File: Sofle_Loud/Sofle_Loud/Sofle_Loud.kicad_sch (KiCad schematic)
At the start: 76 parts, among them J1 Pimaroni Trackball, J2 4PIN, J3 OLED, Q2 TIP120, SW1 SW_PUSH_LED, SW10 SW_PUSH_LED, SW11 SW_PUSH_LED, SW12 SW_PUSH_LED, SW13 SW_PUSH_LED, SW14 SW_PUSH_LED, SW15 SW_PUSH_LED, SW16 SW_PUSH_LED, SW17 SW_PUSH_LED, SW18 SW_PUSH_LED, SW19 SW_PUSH_LED, SW2 SW_PUSH_LED, SW20 SW_PUSH_LED, SW21 SW_PUSH_LED, SW22 SW_PUSH_LED, SW23 SW_PUSH_LED, SW24 SW_PUSH_LED, SW25 Rotary_Encoder_Switch, SW26 SW_PUSH_LED, SW27 SW_PUSH_LED, SW28 SW_PUSH_LED, SW29 SW_PUSH_LED, SW3 SW_PUSH_LED, SW30 SW_PUSH_LED, SW4 SW_PUSH_LED, SW5 SW_PUSH_LED, SW6 SW_PUSH_LED, SW7 SW_PUSH_LED, SW8 SW_PUSH_LED, SW9 SW_PUSH_LED, U1 ProMicro_Choc_MX

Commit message: Updated transistor footprint Added extra room for heatsink Rebuilt outline Wired solenoid and piezzo
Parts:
- Q2: footprint Package_TO_SOT_THT:TO-220-3_Horizontal_TabUp -> SofleChocLoud:TO-220-3_Horizontal_TabUp
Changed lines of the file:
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@@
       (effects (font (size 1.27 1.27)) (justify left))
     )
-    (property "Footprint" "Package_TO_SOT_THT:TO-220-3_Horizontal_TabUp" (at 46.99 135.255 0)
+    (property "Footprint" "SofleChocLoud:TO-220-3_Horizontal_TabUp" (at 46.99 135.255 0)
       (effects (font (size 1.27 1.27) italic) (justify left) hide)
     )

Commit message: Footprint cleanup for plates Added markings to OLEDs indicating screen start/end offset oleds 3mm from edge of board rotated transistor for more slop on heatsinks Created Double sided TRRS footprint Moved Pimaroni closer to OLED footprint diode routing cleanup
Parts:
- J2: footprint SofleChocLoud:MJ-4PP-9_Choc_MX -> SofleChocLoud:TRRS_or_TRS_Sofle_Click
- J_SOL_1: footprint Connector_PinHeader_2.54mm:PinHeader_1x02_P2.54mm_Vertical -> SofleChocLoud:PinHeader_1x02_P2.54mm_L-Shaped
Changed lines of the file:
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@@
       (effects (font (size 1.524 1.524)))
     )
-    (property "Footprint" "SofleChocLoud:MJ-4PP-9_Choc_MX" (at 82.55 78.74 0)
+    (property "Footprint" "SofleChocLoud:TRRS_or_TRS_Sofle_Click" (at 82.55 78.74 0)
       (effects (font (size 1.524 1.524)) hide)
     )
@@
       (effects (font (size 1.27 1.27)))
     )
-    (property "Footprint" "Connector_PinHeader_2.54mm:PinHeader_1x02_P2.54mm_Vertical" (at 30.48 123.19 0)
-      (effects (font (size 1.27 1.27)) hide)
-    )
+    (property "Footprint" "SofleChocLoud:PinHeader_1x02_P2.54mm_L-Shaped" (at 30.48 123.19 0)
+      (effects (font (size 1.27 1.27)) hide)
+    )

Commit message: Adding 2nd tier keyplate
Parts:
- TH1, TH2, TH3, TH4, TH5, TH6, TH7: footprint SofleChocLoud:M2_HOLE_PCB -> SofleChocLoud:M2_HOLE_PCB_through_hole
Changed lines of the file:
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@@
       (effects (font (size 1.524 1.524)))
     )
-    (property "Footprint" "SofleChocLoud:M2_HOLE_PCB" (at 19.05 190.5 0)
+    (property "Footprint" "SofleChocLoud:M2_HOLE_PCB_through_hole" (at 19.05 190.5 0)
       (effects (font (size 1.524 1.524)) hide)
     )
@@
       (effects (font (size 1.524 1.524)))
     )
-    (property "Footprint" "SofleChocLoud:M2_HOLE_PCB" (at 27.94 190.5 0)
+    (property "Footprint" "SofleChocLoud:M2_HOLE_PCB_through_hole" (at 27.94 190.5 0)
       (effects (font (size 1.524 1.524)) hide)
     )
@@
       (effects (font (size 1.524 1.524)))
     )
-    (property "Footprint" "SofleChocLoud:M2_HOLE_PCB" (at 53.34 190.5 0)
+    (property "Footprint" "SofleChocLoud:M2_HOLE_PCB_through_hole" (at 53.34 190.5 0)
       (effects (font (size 1.524 1.524)) hide)
     )
@@
       (effects (font (size 1.524 1.524)))
     )
-    (property "Footprint" "SofleChocLoud:M2_HOLE_PCB" (at 62.23 190.5 0)
+    (property "Footprint" "SofleChocLoud:M2_HOLE_PCB_through_hole" (at 62.23 190.5 0)
       (effects (font (size 1.524 1.524)) hide)
     )
@@
       (effects (font (size 1.524 1.524)))
     )
-    (property "Footprint" "SofleChocLoud:M2_HOLE_PCB" (at 71.12 190.5 0)
+    (property "Footprint" "SofleChocLoud:M2_HOLE_PCB_through_hole" (at 71.12 190.5 0)
       (effects (font (size 1.524 1.524)) hide)
     )
@@
       (effects (font (size 1.524 1.524)))
     )
-    (property "Footprint" "SofleChocLoud:M2_HOLE_PCB" (at 80.01 190.5 0)
+    (property "Footprint" "SofleChocLoud:M2_HOLE_PCB_through_hole" (at 80.01 190.5 0)
       (effects (font (size 1.524 1.524)) hide)
     )
@@
       (effects (font (size 1.524 1.524)))
     )
-    (property "Footprint" "SofleChocLoud:M2_HOLE_PCB" (at 44.45 190.5 0)
+    (property "Footprint" "SofleChocLoud:M2_HOLE_PCB_through_hole" (at 44.45 190.5 0)
       (effects (font (size 1.524 1.524)) hide)
     )

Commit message: Updated pimoroni markings Added 3d models to components
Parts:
- D1, D10, D11, D12, D13, D14, D15, D16, D17, D18, D19, D2, D20, D21, D22, D23, D24, D25, D26, D27, D28, D29, D3, D30, D4, D5, D6, D7, D8, D9: footprint SofleChocLoud:D_SOD-123_DO-35_Hybrid_DoubleSided -> SofleChocLoud:D_SOD-123_DO-35_Hybrid_DoubleSided_V2
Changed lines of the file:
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@@
       (effects (font (size 1.27 1.27)) (justify right))
     )
-    (property "Footprint" "SofleChocLoud:D_SOD-123_DO-35_Hybrid_DoubleSided" (at 175.26 91.44 0)
+    (property "Footprint" "SofleChocLoud:D_SOD-123_DO-35_Hybrid_DoubleSided_V2" (at 175.26 91.44 0)
       (effects (font (size 1.27 1.27)) hide)
     )
@@
       (effects (font (size 1.27 1.27)) (justify right))
     )
-    (property "Footprint" "SofleChocLoud:D_SOD-123_DO-35_Hybrid_DoubleSided" (at 195.58 91.44 0)
+    (property "Footprint" "SofleChocLoud:D_SOD-123_DO-35_Hybrid_DoubleSided_V2" (at 195.58 91.44 0)
       (effects (font (size 1.27 1.27)) hide)
     )
@@
       (effects (font (size 1.27 1.27)) (justify right))
     )
-    (property "Footprint" "SofleChocLoud:D_SOD-123_DO-35_Hybrid_DoubleSided" (at 215.9 91.44 0)
+    (property "Footprint" "SofleChocLoud:D_SOD-123_DO-35_Hybrid_DoubleSided_V2" (at 215.9 91.44 0)
       (effects (font (size 1.27 1.27)) hide)
     )
@@
       (effects (font (size 1.27 1.27)) (justify right))
     )
-    (property "Footprint" "SofleChocLoud:D_SOD-123_DO-35_Hybrid_DoubleSided" (at 236.22 91.44 0)
+    (property "Footprint" "SofleChocLoud:D_SOD-123_DO-35_Hybrid_DoubleSided_V2" (at 236.22 91.44 0)
       (effects (font (size 1.27 1.27)) hide)
     )
@@
       (effects (font (size 1.27 1.27)) (justify right))
     )
-    (property "Footprint" "SofleChocLoud:D_SOD-123_DO-35_Hybrid_DoubleSided" (at 256.54 91.44 0)
+    (property "Footprint" "SofleChocLoud:D_SOD-123_DO-35_Hybrid_DoubleSided_V2" (at 256.54 91.44 0)
       (effects (font (size 1.27 1.27)) hide)
     )
@@
       (effects (font (size 1.27 1.27)) (justify right))
     )
-    (property "Footprint" "SofleChocLoud:D_SOD-123_DO-35_Hybrid_DoubleSided" (at 276.86 91.44 0)
+    (property "Footprint" "SofleChocLoud:D_SOD-123_DO-35_Hybrid_DoubleSided_V2" (at 276.86 91.44 0)
       (effects (font (size 1.27 1.27)) hide)
     )
@@
       (effects (font (size 1.27 1.27)) (justify right))
     )
-    (property "Footprint" "SofleChocLoud:D_SOD-123_DO-35_Hybrid_DoubleSided" (at 175.26 107.95 0)
+    (property "Footprint" "SofleChocLoud:D_SOD-123_DO-35_Hybrid_DoubleSided_V2" (at 175.26 107.95 0)
       (effects (font (size 1.27 1.27)) hide)
     )
@@
       (effects (font (size 1.27 1.27)) (justify right))
     )
-    (property "Footprint" "SofleChocLoud:D_SOD-123_DO-35_Hybrid_DoubleSided" (at 195.58 107.95 0)
+    (property "Footprint" "SofleChocLoud:D_SOD-123_DO-35_Hybrid_DoubleSided_V2" (at 195.58 107.95 0)
       (effects (font (size 1.27 1.27)) hide)
     )
@@
       (effects (font (size 1.27 1.27)) (justify right))
     )
-    (property "Footprint" "SofleChocLoud:D_SOD-123_DO-35_Hybrid_DoubleSided" (at 215.9 107.95 0)
+    (property "Footprint" "SofleChocLoud:D_SOD-123_DO-35_Hybrid_DoubleSided_V2" (at 215.9 107.95 0)
       (effects (font (size 1.27 1.27)) hide)
     )
@@
       (effects (font (size 1.27 1.27)) (justify right))
     )
-    (property "Footprint" "SofleChocLoud:D_SOD-123_DO-35_Hybrid_DoubleSided" (at 236.22 107.95 0)
+    (property "Footprint" "SofleChocLoud:D_SOD-123_DO-35_Hybrid_DoubleSided_V2" (at 236.22 107.95 0)
       (effects (font (size 1.27 1.27)) hide)
     )
@@
       (effects (font (size 1.27 1.27)) (justify right))
     )
-    (property "Footprint" "SofleChocLoud:D_SOD-123_DO-35_Hybrid_DoubleSided" (at 256.54 107.95 0)
+    (property "Footprint" "SofleChocLoud:D_SOD-123_DO-35_Hybrid_DoubleSided_V2" (at 256.54 107.95 0)
       (effects (font (size 1.27 1.27)) hide)
     )
@@
       (effects (font (size 1.27 1.27)) (justify right))
     )
-    (property "Footprint" "SofleChocLoud:D_SOD-123_DO-35_Hybrid_DoubleSided" (at 276.86 107.95 0)
+    (property "Footprint" "SofleChocLoud:D_SOD-123_DO-35_Hybrid_DoubleSided_V2" (at 276.86 107.95 0)
       (effects (font (size 1.27 1.27)) hide)
     )
@@
       (effects (font (size 1.27 1.27)) (justify right))
     )
-    (property "Footprint" "SofleChocLoud:D_SOD-123_DO-35_Hybrid_DoubleSided" (at 175.26 124.46 0)
+    (property "Footprint" "SofleChocLoud:D_SOD-123_DO-35_Hybrid_DoubleSided_V2" (at 175.26 124.46 0)
       (effects (font (size 1.27 1.27)) hide)
     )
@@
       (effects (font (size 1.27 1.27)) (justify right))
     )
-    (property "Footprint" "SofleChocLoud:D_SOD-123_DO-35_Hybrid_DoubleSided" (at 195.58 124.46 0)
+    (property "Footprint" "SofleChocLoud:D_SOD-123_DO-35_Hybrid_DoubleSided_V2" (at 195.58 124.46 0)
       (effects (font (size 1.27 1.27)) hide)
     )
@@
       (effects (font (size 1.27 1.27)) (justify right))
     )
-    (property "Footprint" "SofleChocLoud:D_SOD-123_DO-35_Hybrid_DoubleSided" (at 215.9 124.46 0)
+    (property "Footprint" "SofleChocLoud:D_SOD-123_DO-35_Hybrid_DoubleSided_V2" (at 215.9 124.46 0)
       (effects (font (size 1.27 1.27)) hide)
     )
@@
       (effects (font (size 1.27 1.27)) (justify right))
     )
-    (property "Footprint" "SofleChocLoud:D_SOD-123_DO-35_Hybrid_DoubleSided" (at 236.22 124.46 0)
+    (property "Footprint" "SofleChocLoud:D_SOD-123_DO-35_Hybrid_DoubleSided_V2" (at 236.22 124.46 0)
       (effects (font (size 1.27 1.27)) hide)
     )
@@
       (effects (font (size 1.27 1.27)) (justify right))
     )
-    (property "Footprint" "SofleChocLoud:D_SOD-123_DO-35_Hybrid_DoubleSided" (at 256.54 124.46 0)
+    (property "Footprint" "SofleChocLoud:D_SOD-123_DO-35_Hybrid_DoubleSided_V2" (at 256.54 124.46 0)
       (effects (font (size 1.27 1.27)) hide)
     )
@@
       (effects (font (size 1.27 1.27)) (justify right))
     )
-    (property "Footprint" "SofleChocLoud:D_SOD-123_DO-35_Hybrid_DoubleSided" (at 276.86 124.46 0)
+    (property "Footprint" "SofleChocLoud:D_SOD-123_DO-35_Hybrid_DoubleSided_V2" (at 276.86 124.46 0)
       (effects (font (size 1.27 1.27)) hide)
     )
@@
       (effects (font (size 1.27 1.27)) (justify right))
     )
-    (property "Footprint" "SofleChocLoud:D_SOD-123_DO-35_Hybrid_DoubleSided" (at 175.26 140.97 0)
+    (property "Footprint" "SofleChocLoud:D_SOD-123_DO-35_Hybrid_DoubleSided_V2" (at 175.26 140.97 0)
       (effects (font (size 1.27 1.27)) hide)
     )
@@
       (effects (font (size 1.27 1.27)) (justify right))
     )
-    (property "Footprint" "SofleChocLoud:D_SOD-123_DO-35_Hybrid_DoubleSided" (at 195.58 140.97 0)
+    (property "Footprint" "SofleChocLoud:D_SOD-123_DO-35_Hybrid_DoubleSided_V2" (at 195.58 140.97 0)
       (effects (font (size 1.27 1.27)) hide)
     )
@@
       (effects (font (size 1.27 1.27)) (justify right))
     )
-    (property "Footprint" "SofleChocLoud:D_SOD-123_DO-35_Hybrid_DoubleSided" (at 215.9 140.97 0)
+    (property "Footprint" "SofleChocLoud:D_SOD-123_DO-35_Hybrid_DoubleSided_V2" (at 215.9 140.97 0)
       (effects (font (size 1.27 1.27)) hide)
     )
@@
       (effects (font (size 1.27 1.27)) (justify right))
     )
-    (property "Footprint" "SofleChocLoud:D_SOD-123_DO-35_Hybrid_DoubleSided" (at 236.22 140.97 0)
+    (property "Footprint" "SofleChocLoud:D_SOD-123_DO-35_Hybrid_DoubleSided_V2" (at 236.22 140.97 0)
       (effects (font (size 1.27 1.27)) hide)
     )
@@
       (effects (font (size 1.27 1.27)) (justify right))
     )
-    (property "Footprint" "SofleChocLoud:D_SOD-123_DO-35_Hybrid_DoubleSided" (at 256.54 140.97 0)
+    (property "Footprint" "SofleChocLoud:D_SOD-123_DO-35_Hybrid_DoubleSided_V2" (at 256.54 140.97 0)
       (effects (font (size 1.27 1.27)) hide)
     )
@@
       (effects (font (size 1.27 1.27)) (justify right))
     )
-    (property "Footprint" "SofleChocLoud:D_SOD-123_DO-35_Hybrid_DoubleSided" (at 276.86 140.97 0)
+    (property "Footprint" "SofleChocLoud:D_SOD-123_DO-35_Hybrid_DoubleSided_V2" (at 276.86 140.97 0)
       (effects (font (size 1.27 1.27)) hide)
     )
@@
       (effects (font (size 1.27 1.27)) (justify right))
     )
-    (property "Footprint" "SofleChocLoud:D_SOD-123_DO-35_Hybrid_DoubleSided" (at 175.26 157.48 0)
+    (property "Footprint" "SofleChocLoud:D_SOD-123_DO-35_Hybrid_DoubleSided_V2" (at 175.26 157.48 0)
       (effects (font (size 1.27 1.27)) hide)
     )
@@
       (effects (font (size 1.27 1.27)) (justify right))
     )
-    (property "Footprint" "SofleChocLoud:D_SOD-123_DO-35_Hybrid_DoubleSided" (at 195.58 157.48 0)
+    (property "Footprint" "SofleChocLoud:D_SOD-123_DO-35_Hybrid_DoubleSided_V2" (at 195.58 157.48 0)
       (effects (font (size 1.27 1.27)) hide)
     )
@@
       (effects (font (size 1.27 1.27)) (justify right))
     )
-    (property "Footprint" "SofleChocLoud:D_SOD-123_DO-35_Hybrid_DoubleSided" (at 215.9 157.48 0)
+    (property "Footprint" "SofleChocLoud:D_SOD-123_DO-35_Hybrid_DoubleSided_V2" (at 215.9 157.48 0)
       (effects (font (size 1.27 1.27)) hide)
     )
@@
       (effects (font (size 1.27 1.27)) (justify right))
     )
-    (property "Footprint" "SofleChocLoud:D_SOD-123_DO-35_Hybrid_DoubleSided" (at 236.22 157.48 0)
+    (property "Footprint" "SofleChocLoud:D_SOD-123_DO-35_Hybrid_DoubleSided_V2" (at 236.22 157.48 0)
       (effects (font (size 1.27 1.27)) hide)
     )
@@
       (effects (font (size 1.27 1.27)) (justify right))
     )
-    (property "Footprint" "SofleChocLoud:D_SOD-123_DO-35_Hybrid_DoubleSided" (at 256.54 157.48 0)
+    (property "Footprint" "SofleChocLoud:D_SOD-123_DO-35_Hybrid_DoubleSided_V2" (at 256.54 157.48 0)
       (effects (font (size 1.27 1.27)) hide)
     )
@@
       (effects (font (size 1.27 1.27)) (justify right))
     )
-    (property "Footprint" "SofleChocLoud:D_SOD-123_DO-35_Hybrid_DoubleSided" (at 276.86 157.48 0)
-      (effects (font (size 1.27 1.27)) hide)
-    )
+    (property "Footprint" "SofleChocLoud:D_SOD-123_DO-35_Hybrid_DoubleSided_V2" (at 276.86 157.48 0)
+      (effects (font (size 1.27 1.27)) hide)
+    )

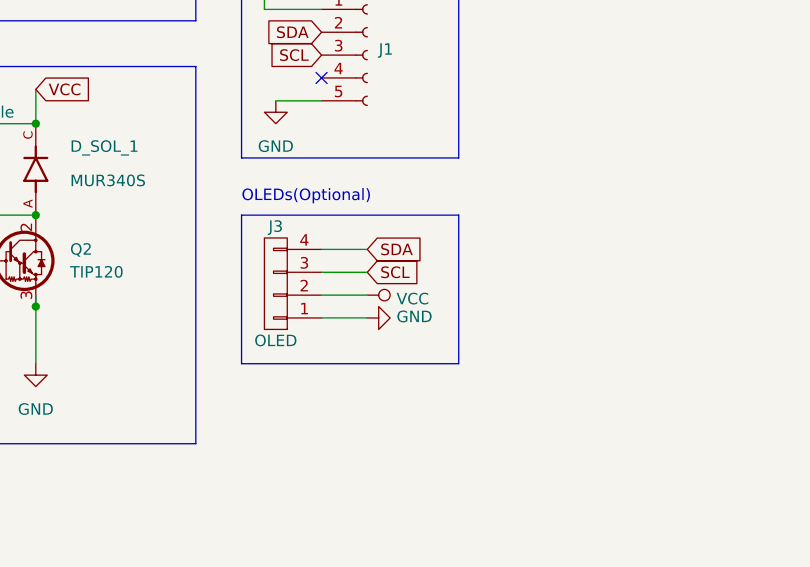
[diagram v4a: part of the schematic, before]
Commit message: Fixed reveresed OLED pins
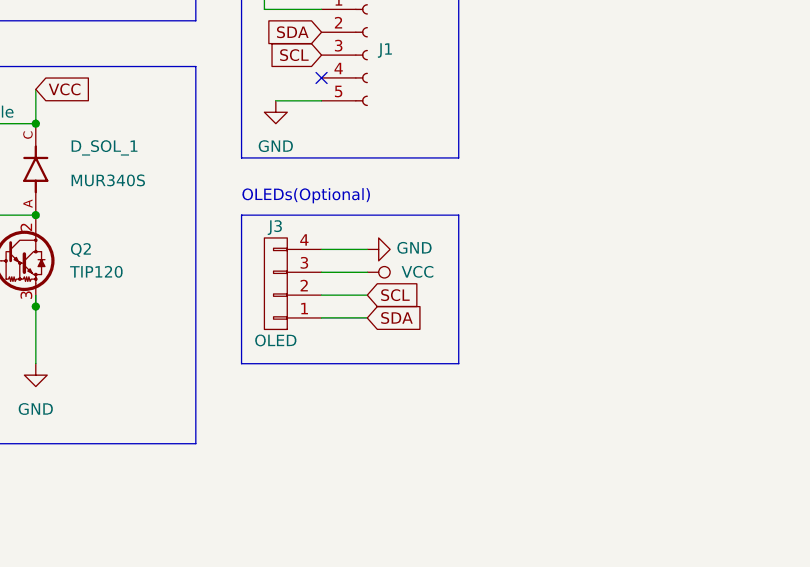
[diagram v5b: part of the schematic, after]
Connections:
- net GND: now also J3.4 (P4); no longer J3.1 (P1)
- net SCL: now also J3.2 (P2); no longer J3.3 (P3)
- net SDA: now also J3.1 (P1); no longer J3.4 (P4)
- net VCC: now also J3.3 (P3); no longer J3.2 (P2)
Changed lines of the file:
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@@
     (effects (font (size 1.27 1.27)) (justify left bottom))
   )
+  (global_label "SDA" (shape input) (at 81.28 139.7 0)
+    (effects (font (size 1.27 1.27)) (justify left))
+    (property "Intersheetrefs" "${INTERSHEET_REFS}" (at 81.28 139.7 0)
+      (effects (font (size 1.27 1.27)) hide)
+    )
+  )
+  (global_label "SCL" (shape input) (at 81.28 137.16 0)
+    (effects (font (size 1.27 1.27)) (justify left))
+    (property "Intersheetrefs" "${INTERSHEET_REFS}" (at 81.28 137.16 0)
+      (effects (font (size 1.27 1.27)) hide)
+    )
+  )
   (global_label "VCC" (shape input) (at 44.45 114.3 0) (fields_autoplaced)
     (effects (font (size 1.27 1.27)) (justify left))
@@
     )
   )
-  (global_label "SDA" (shape input) (at 81.28 132.08 0)
-    (effects (font (size 1.27 1.27)) (justify left))
-    (property "Intersheetrefs" "${INTERSHEET_REFS}" (at 81.28 132.08 0)
-      (effects (font (size 1.27 1.27)) hide)
-    )
-  )
-  (global_label "SCL" (shape input) (at 81.28 134.62 0)
-    (effects (font (size 1.27 1.27)) (justify left))
-    (property "Intersheetrefs" "${INTERSHEET_REFS}" (at 81.28 134.62 0)
-      (effects (font (size 1.27 1.27)) hide)
-    )
-  )
   (global_label "col5" (shape input) (at 60.96 49.53 0)
     (effects (font (size 1.27 1.27)) (justify left))
@@
     )
   )
+  (symbol (lib_id "SofleKeyboard-rescue:GND-power") (at 81.28 132.08 90) (unit 1)
+    (in_bom yes) (on_board yes) (dnp no)
+    (property "Reference" "#PWR03" (at 87.63 132.08 0)
+      (effects (font (size 1.27 1.27)) hide)
+    )
+    (property "Value" "GND" (at 84.5312 131.953 90)
+      (effects (font (size 1.27 1.27)) (justify right))
+    )
+    (property "Footprint" "" (at 81.28 132.08 0)
+      (effects (font (size 1.27 1.27)) hide)
+    )
+    (property "Datasheet" "" (at 81.28 132.08 0)
+      (effects (font (size 1.27 1.27)) hide)
+    )
+    (pin "1")
+    (instances
+      (project "Sofle_Loud"
+        (path "/06057b3a-55ab-4f4e-913e-2aeec5ff3587"
+          (reference "#PWR03") (unit 1)
+        )
+      )
+    )
+  )
   (symbol (lib_id "Connector:Conn_01x02_Female") (at 30.48 123.19 180) (unit 1)
     (in_bom yes) (on_board yes) (dnp no)
@@
     )
   )
-  (symbol (lib_id "SofleKeyboard-rescue:VCC-power") (at 81.28 137.16 270) (unit 1)
+  (symbol (lib_id "SofleKeyboard-rescue:VCC-power") (at 81.28 134.62 270) (unit 1)
     (in_bom yes) (on_board yes) (dnp no)
-    (property "Reference" "#PWR09" (at 77.47 137.16 0)
+    (property "Reference" "#PWR05" (at 77.47 134.62 0)
       (effects (font (size 1.27 1.27)) hide)
     )
-    (property "Value" "VCC" (at 84.5312 137.5918 90)
+    (property "Value" "VCC" (at 85.09 134.62 90)
       (effects (font (size 1.27 1.27)) (justify left))
     )
-    (property "Footprint" "" (at 81.28 137.16 0)
+    (property "Footprint" "" (at 81.28 134.62 0)
       (effects (font (size 1.27 1.27)) hide)
     )
-    (property "Datasheet" "" (at 81.28 137.16 0)
+    (property "Datasheet" "" (at 81.28 134.62 0)
       (effects (font (size 1.27 1.27)) hide)
     )
@@
       (project "Sofle_Loud"
         (path "/06057b3a-55ab-4f4e-913e-2aeec5ff3587"
-          (reference "#PWR09") (unit 1)
+          (reference "#PWR05") (unit 1)
         )
       )
@@
         )
       )
-    )
-  )
-  (symbol (lib_id "SofleKeyboard-rescue:GND-power") (at 81.28 139.7 90) (unit 1)
-    (in_bom yes) (on_board yes) (dnp no)
-    (property "Reference" "#PWR03" (at 87.63 139.7 0)
-      (effects (font (size 1.27 1.27)) hide)
-    )
-    (property "Value" "GND" (at 84.5312 139.573 90)
-      (effects (font (size 1.27 1.27)) (justify right))
-    )
-    (property "Footprint" "" (at 81.28 139.7 0)
-      (effects (font (size 1.27 1.27)) hide)
-    )
-    (property "Datasheet" "" (at 81.28 139.7 0)
-      (effects (font (size 1.27 1.27)) hide)
-    )
-    (pin "1")
-    (instances
-      (project "Sofle_Loud"
-        (path "/06057b3a-55ab-4f4e-913e-2aeec5ff3587"
-          (reference "#PWR03") (unit 1)
-        )
-      )
